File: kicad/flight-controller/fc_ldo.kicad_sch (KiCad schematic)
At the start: 6 parts, among them U5 AP2112K-3.3, U6 AP2112K-3.3

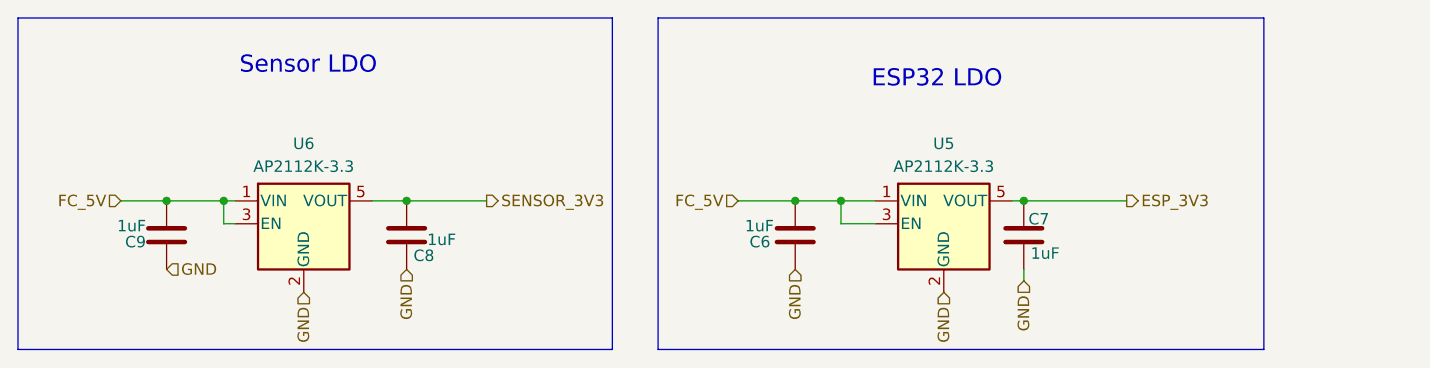
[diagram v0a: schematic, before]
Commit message: Fix ESP32 LDO thermal margin, add USB-C/SBUS ESD protection
Design review flagged the ESP32-S3's 3.3V LDO (AP2112K-3.3, SOT-23-5)
at only 1.5C margin to absolute max under WiFi load. Swapped to a
Torex XC6220B331PR-G (SOT-89-5, thermal tab tied to GND) with matching
input/output caps and thermal vias under the tab; thermal score is now
100/100 with no findings. Sensor LDO (U6) was unaffected and left as-is.

Also added TVS protection that was missing on two exposed signal paths:
D4 + bulk cap on USB-C VBUS (J13, now populated for field use) ahead of
the existing blocking diode, and a matching TVS (D6) on the RC receiver
SBUS line (J7), reusing the same part to minimize BOM diversity.

Every part number touched this pass (U4, C17-C19, D4, D6) was verified
against real distributor data, and a full BOM audit confirmed all other
assigned part numbers match their stated value and footprint. Also
removed two orphaned, unwired schematic files (airspeed.kicad_sch,
lidar.kicad_sch) that weren't in the sheet hierarchy.

Known follow-up before fab: the production/ fab package predates this
rework and needs to be regenerated, and Update PCB from Schematic needs
a re-run to sync D4/D6's display value (nets are already correct).

Co-Authored-By: Claude Sonnet 5 <noreply@anthropic.com>
Claude-Session: https://claude.ai/code/session_01NksRnW4jXLWsYwZNR7u39H
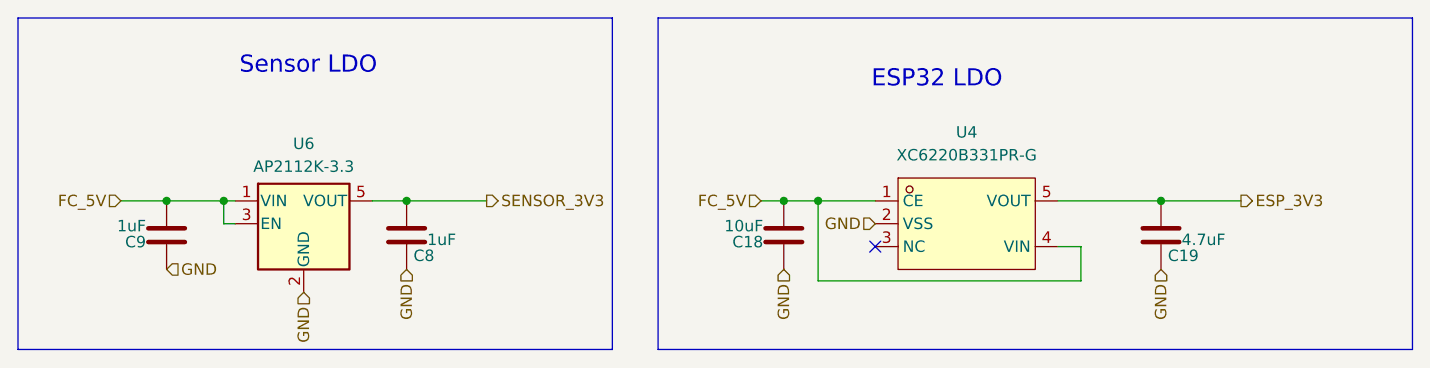
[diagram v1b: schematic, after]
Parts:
- removed C6, C7: 1uF, Capacitor_SMD:C_0402_1005Metric, symbol Device:C
- removed U5: AP2112K-3.3, Package_TO_SOT_SMD:SOT-23-5, symbol Regulator_Linear:AP2112K-3.3
- added C18: 10uF, Capacitor_SMD:C_0603_1608Metric, symbol Device:C
- added C19: 4.7uF, Capacitor_SMD:C_0603_1608Metric, symbol Device:C
- added U4: XC6220B331PR-G, easyeda2kicad:SOT-89-5_L4.5-W2.5-P1.50-LS4.4-BR, symbol easyeda2kicad:XC6220B331PR-G
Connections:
- net ESP_3V3: now also C19.1, U4.5 (VOUT)
- net FC_5V: now also C18.2, U4.1 (CE), U4.4 (VIN)
- net GND: now also C18.1, C19.2, U4.2 (VSS)
- no-connect marks 0 -> 1
